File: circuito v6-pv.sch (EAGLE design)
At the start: 62 parts, among them IC1 LM324N

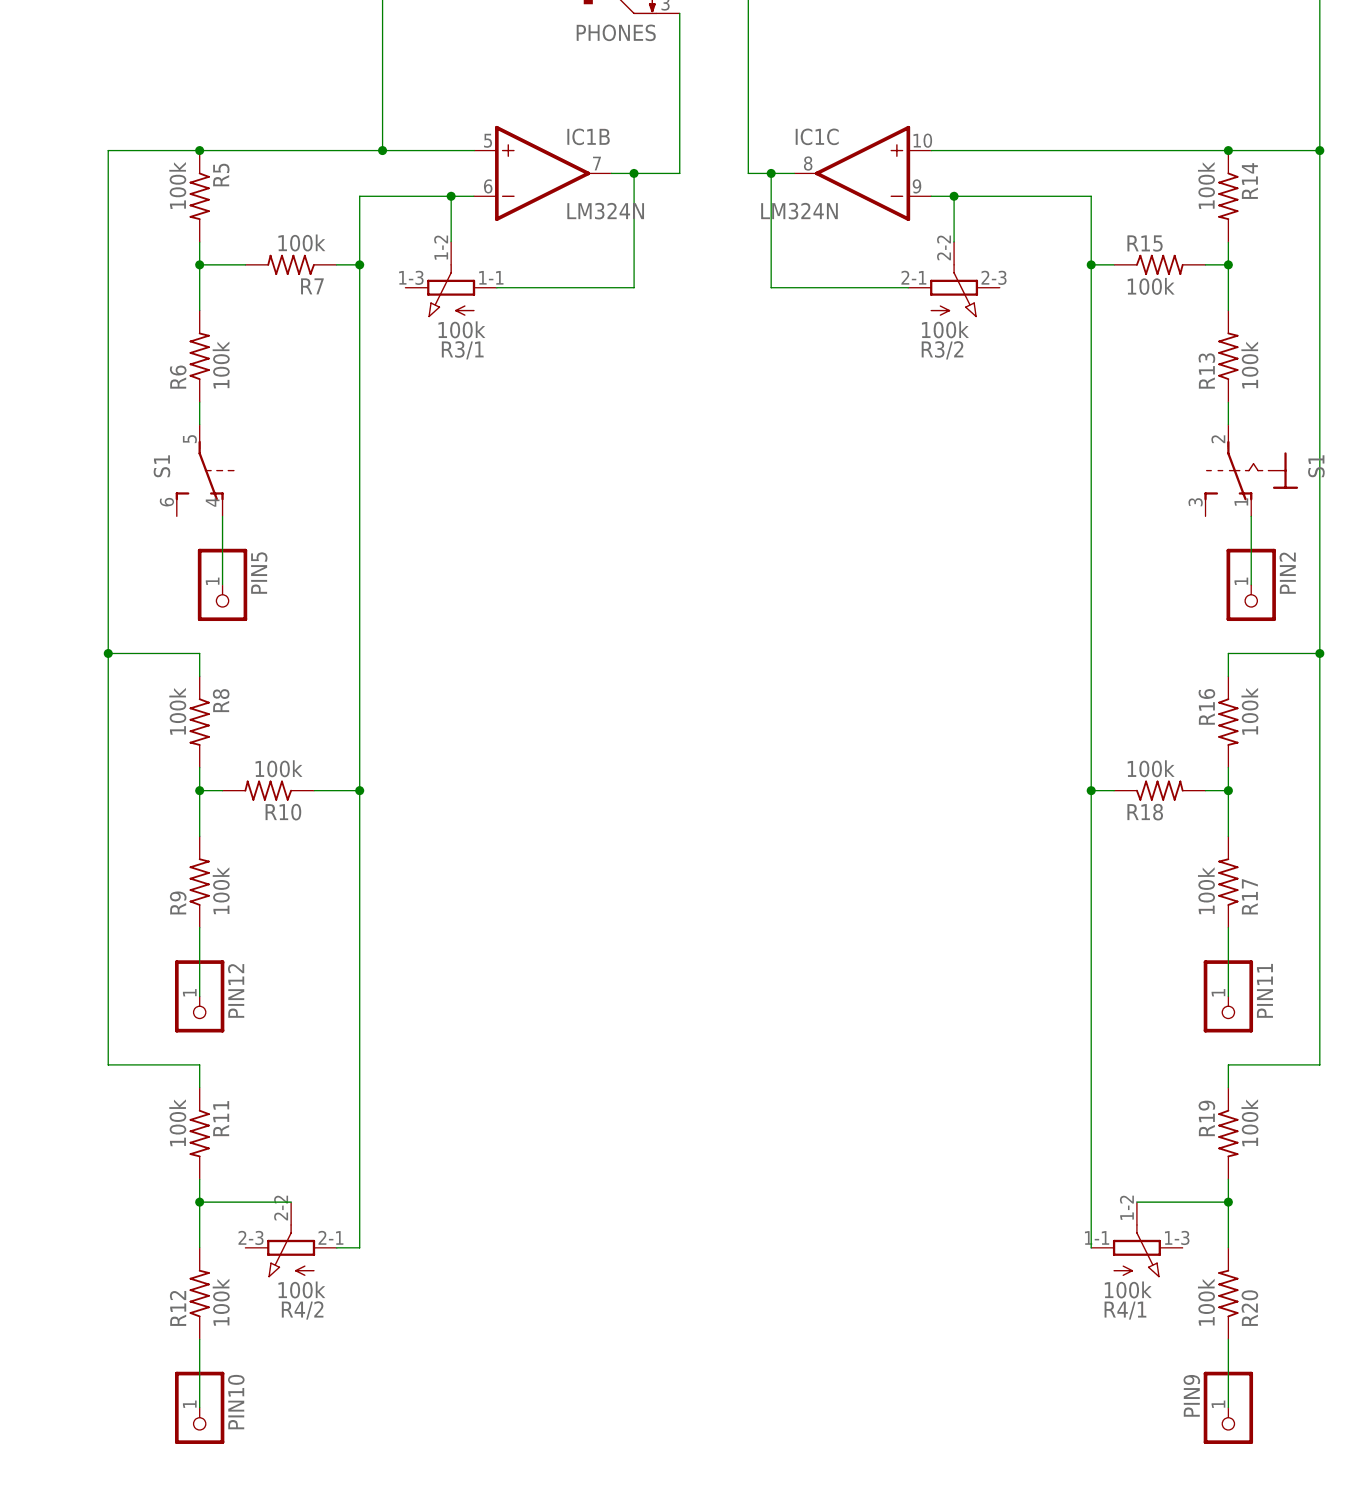
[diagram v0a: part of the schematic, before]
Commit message: Cambio de resistencias de 100k a 10k
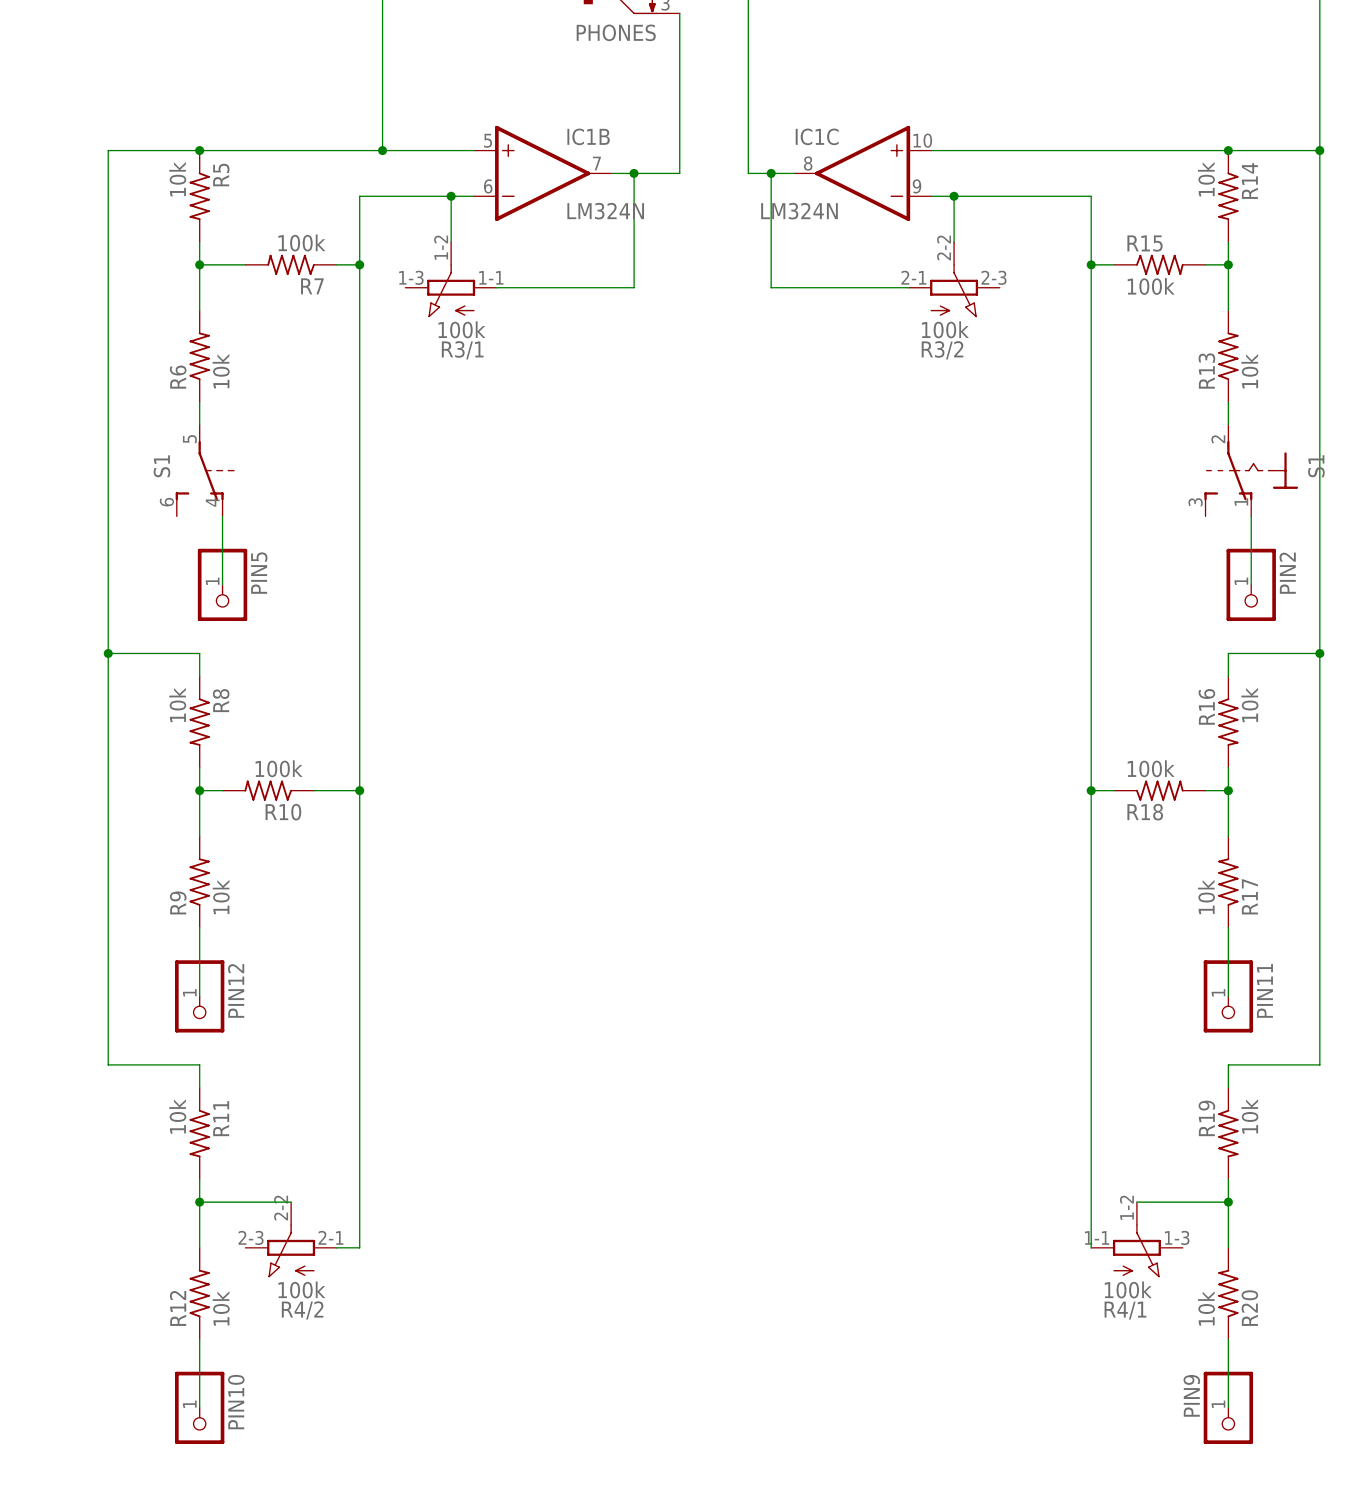
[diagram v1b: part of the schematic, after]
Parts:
- R11, R12, R13, R14, R16, R17, R19, R20, R5, R6, R8, R9: value 100k -> 10k
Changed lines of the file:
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@@
 <attribute name="SPICEPREFIX" value="J"/>
 </part>
-<part name="R5" library="rcl" library_urn="urn:adsk.eagle:library:334" deviceset="R-US_" device="0207/7" package3d_urn="urn:adsk.eagle:package:23493/1" value="100k">
+<part name="R5" library="rcl" library_urn="urn:adsk.eagle:library:334" deviceset="R-US_" device="0207/7" package3d_urn="urn:adsk.eagle:package:23493/1" value="10k">
 <spice>
 <pinmapping isusermap="yes" isdevicewide="yes">
@@
 </spice>
 </part>
-<part name="R6" library="rcl" library_urn="urn:adsk.eagle:library:334" deviceset="R-US_" device="0207/7" package3d_urn="urn:adsk.eagle:package:23493/1" value="100k">
+<part name="R6" library="rcl" library_urn="urn:adsk.eagle:library:334" deviceset="R-US_" device="0207/7" package3d_urn="urn:adsk.eagle:package:23493/1" value="10k">
 <spice>
 <pinmapping isusermap="yes" isdevicewide="yes">
@@
 <attribute name="SPICEPREFIX" value="X"/>
 </part>
-<part name="R8" library="rcl" library_urn="urn:adsk.eagle:library:334" deviceset="R-US_" device="0207/7" package3d_urn="urn:adsk.eagle:package:23493/1" value="100k">
+<part name="R8" library="rcl" library_urn="urn:adsk.eagle:library:334" deviceset="R-US_" device="0207/7" package3d_urn="urn:adsk.eagle:package:23493/1" value="10k">
 <spice>
 <pinmapping isusermap="yes" isdevicewide="yes">
@@
 </spice>
 </part>
-<part name="R9" library="rcl" library_urn="urn:adsk.eagle:library:334" deviceset="R-US_" device="0207/7" package3d_urn="urn:adsk.eagle:package:23493/1" value="100k">
+<part name="R9" library="rcl" library_urn="urn:adsk.eagle:library:334" deviceset="R-US_" device="0207/7" package3d_urn="urn:adsk.eagle:package:23493/1" value="10k">
 <spice>
 <pinmapping isusermap="yes" isdevicewide="yes">
@@
 <attribute name="SPICEPREFIX" value="X"/>
 </part>
-<part name="R11" library="rcl" library_urn="urn:adsk.eagle:library:334" deviceset="R-US_" device="0207/7" package3d_urn="urn:adsk.eagle:package:23493/1" value="100k">
+<part name="R11" library="rcl" library_urn="urn:adsk.eagle:library:334" deviceset="R-US_" device="0207/7" package3d_urn="urn:adsk.eagle:package:23493/1" value="10k">
 <spice>
 <pinmapping isusermap="yes" isdevicewide="yes">
@@
 </spice>
 </part>
-<part name="R12" library="rcl" library_urn="urn:adsk.eagle:library:334" deviceset="R-US_" device="0207/7" package3d_urn="urn:adsk.eagle:package:23493/1" value="100k">
+<part name="R12" library="rcl" library_urn="urn:adsk.eagle:library:334" deviceset="R-US_" device="0207/7" package3d_urn="urn:adsk.eagle:package:23493/1" value="10k">
 <spice>
 <pinmapping isusermap="yes" isdevicewide="yes">
@@
 <attribute name="SPICEPREFIX" value="X"/>
 </part>
-<part name="R13" library="rcl" library_urn="urn:adsk.eagle:library:334" deviceset="R-US_" device="0207/7" package3d_urn="urn:adsk.eagle:package:23493/1" value="100k">
+<part name="R13" library="rcl" library_urn="urn:adsk.eagle:library:334" deviceset="R-US_" device="0207/7" package3d_urn="urn:adsk.eagle:package:23493/1" value="10k">
 <spice>
 <pinmapping isusermap="yes" isdevicewide="yes">
@@
 </spice>
 </part>
-<part name="R14" library="rcl" library_urn="urn:adsk.eagle:library:334" deviceset="R-US_" device="0207/7" package3d_urn="urn:adsk.eagle:package:23493/1" value="100k">
+<part name="R14" library="rcl" library_urn="urn:adsk.eagle:library:334" deviceset="R-US_" device="0207/7" package3d_urn="urn:adsk.eagle:package:23493/1" value="10k">
 <spice>
 <pinmapping isusermap="yes" isdevicewide="yes">
@@
 <attribute name="SPICEPREFIX" value="X"/>
 </part>
-<part name="R16" library="rcl" library_urn="urn:adsk.eagle:library:334" deviceset="R-US_" device="0207/7" package3d_urn="urn:adsk.eagle:package:23493/1" value="100k">
+<part name="R16" library="rcl" library_urn="urn:adsk.eagle:library:334" deviceset="R-US_" device="0207/7" package3d_urn="urn:adsk.eagle:package:23493/1" value="10k">
 <spice>
 <pinmapping isusermap="yes" isdevicewide="yes">
@@
 </spice>
 </part>
-<part name="R17" library="rcl" library_urn="urn:adsk.eagle:library:334" deviceset="R-US_" device="0207/7" package3d_urn="urn:adsk.eagle:package:23493/1" value="100k">
+<part name="R17" library="rcl" library_urn="urn:adsk.eagle:library:334" deviceset="R-US_" device="0207/7" package3d_urn="urn:adsk.eagle:package:23493/1" value="10k">
 <spice>
 <pinmapping isusermap="yes" isdevicewide="yes">
@@
 <attribute name="SPICEPREFIX" value="X"/>
 </part>
-<part name="R19" library="rcl" library_urn="urn:adsk.eagle:library:334" deviceset="R-US_" device="0207/7" package3d_urn="urn:adsk.eagle:package:23493/1" value="100k">
+<part name="R19" library="rcl" library_urn="urn:adsk.eagle:library:334" deviceset="R-US_" device="0207/7" package3d_urn="urn:adsk.eagle:package:23493/1" value="10k">
 <spice>
 <pinmapping isusermap="yes" isdevicewide="yes">
@@
 </spice>
 </part>
-<part name="R20" library="rcl" library_urn="urn:adsk.eagle:library:334" deviceset="R-US_" device="0207/7" package3d_urn="urn:adsk.eagle:package:23493/1" value="100k">
+<part name="R20" library="rcl" library_urn="urn:adsk.eagle:library:334" deviceset="R-US_" device="0207/7" package3d_urn="urn:adsk.eagle:package:23493/1" value="10k">
 <spice>
 <pinmapping isusermap="yes" isdevicewide="yes">

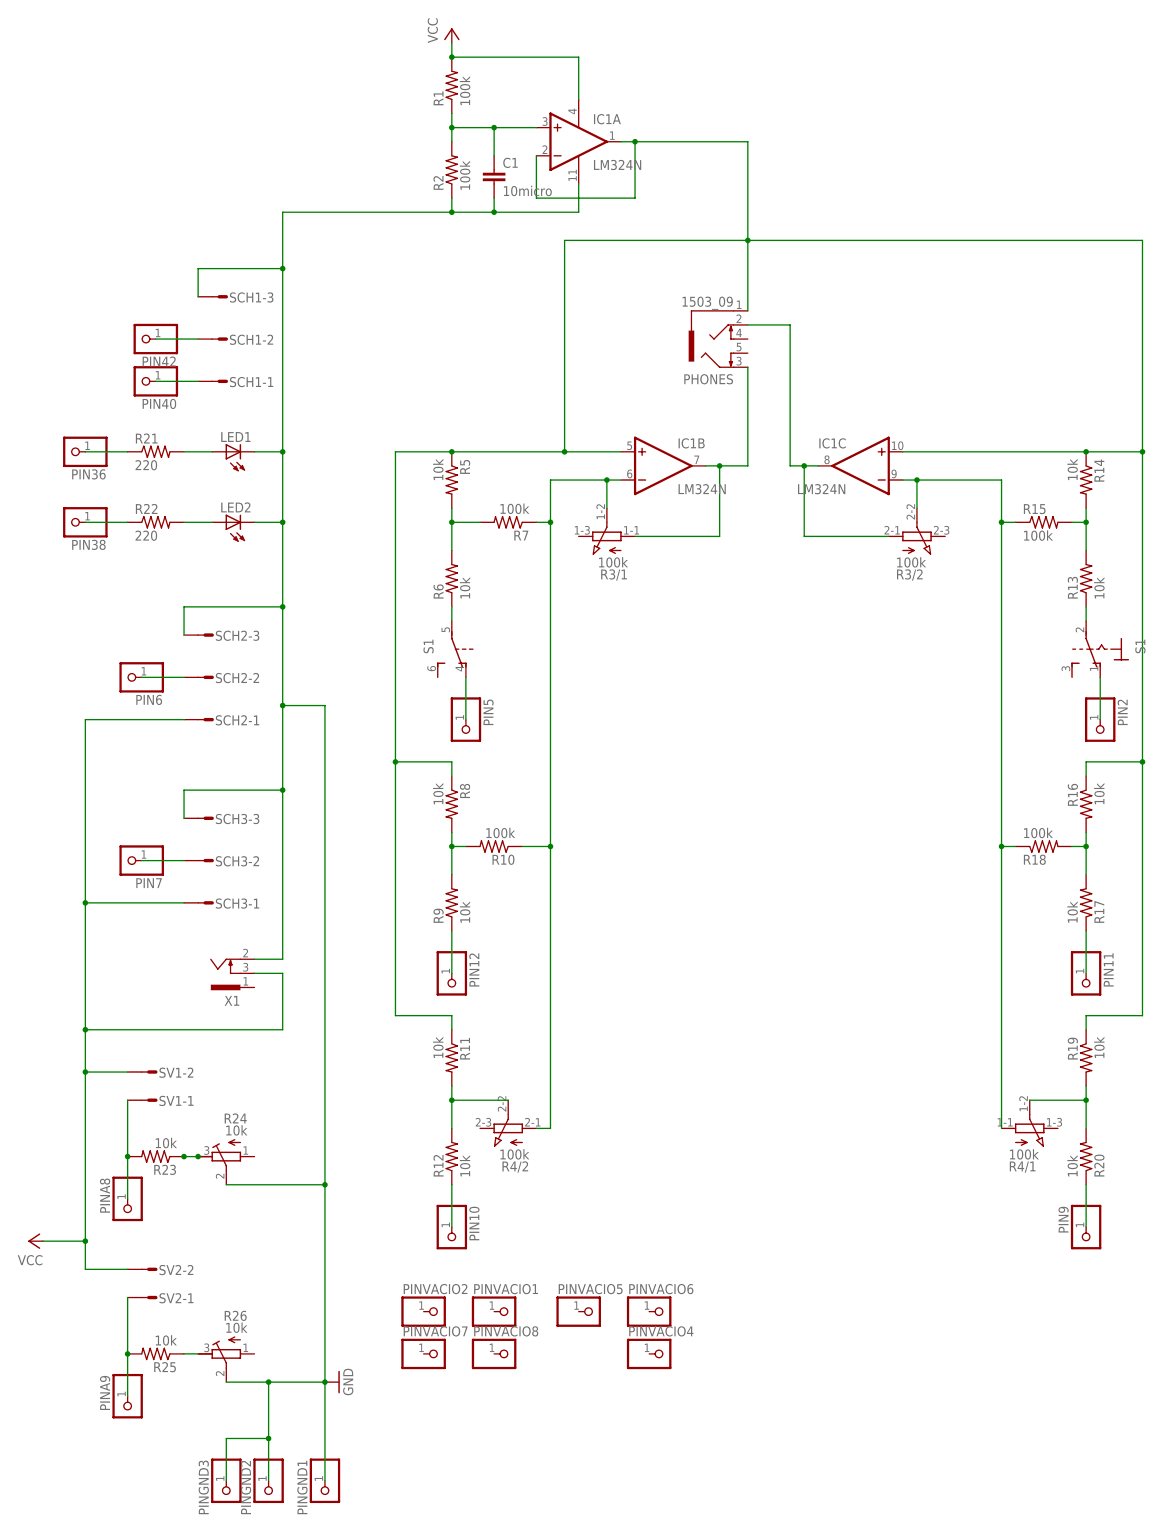
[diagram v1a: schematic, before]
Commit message: ACTUALIZACION CIRCUITO
Cambios

1- Chequeo de pines/canales/izq y der: 

IZQ - B - 12,9 Y 2
DER - A - 11,10Y5

2- CONEXION TIERRA VIRTUAL A PIN A11

3- CAMBIO DE RESISTENCIAS PARA EL PIN DEL RUIDO

EL POTE PASA A SER DOS Rs DE 100K FIJAS
R11 Y R19 TENIAN 10K Y AHORA TIENEN 1K
R12 Y R20 TENIAN 10K Y AHORA TIENEN 20K

4- SE AGREGAN RESISTENCIAS EN LAS PATAS + DE LOS OPAMPS DE AUDIO (IZQ Y DER)

UNA A TIERRA VIRTUAL DE 10K
OTRA A TIERRA NORMAL DE 100K
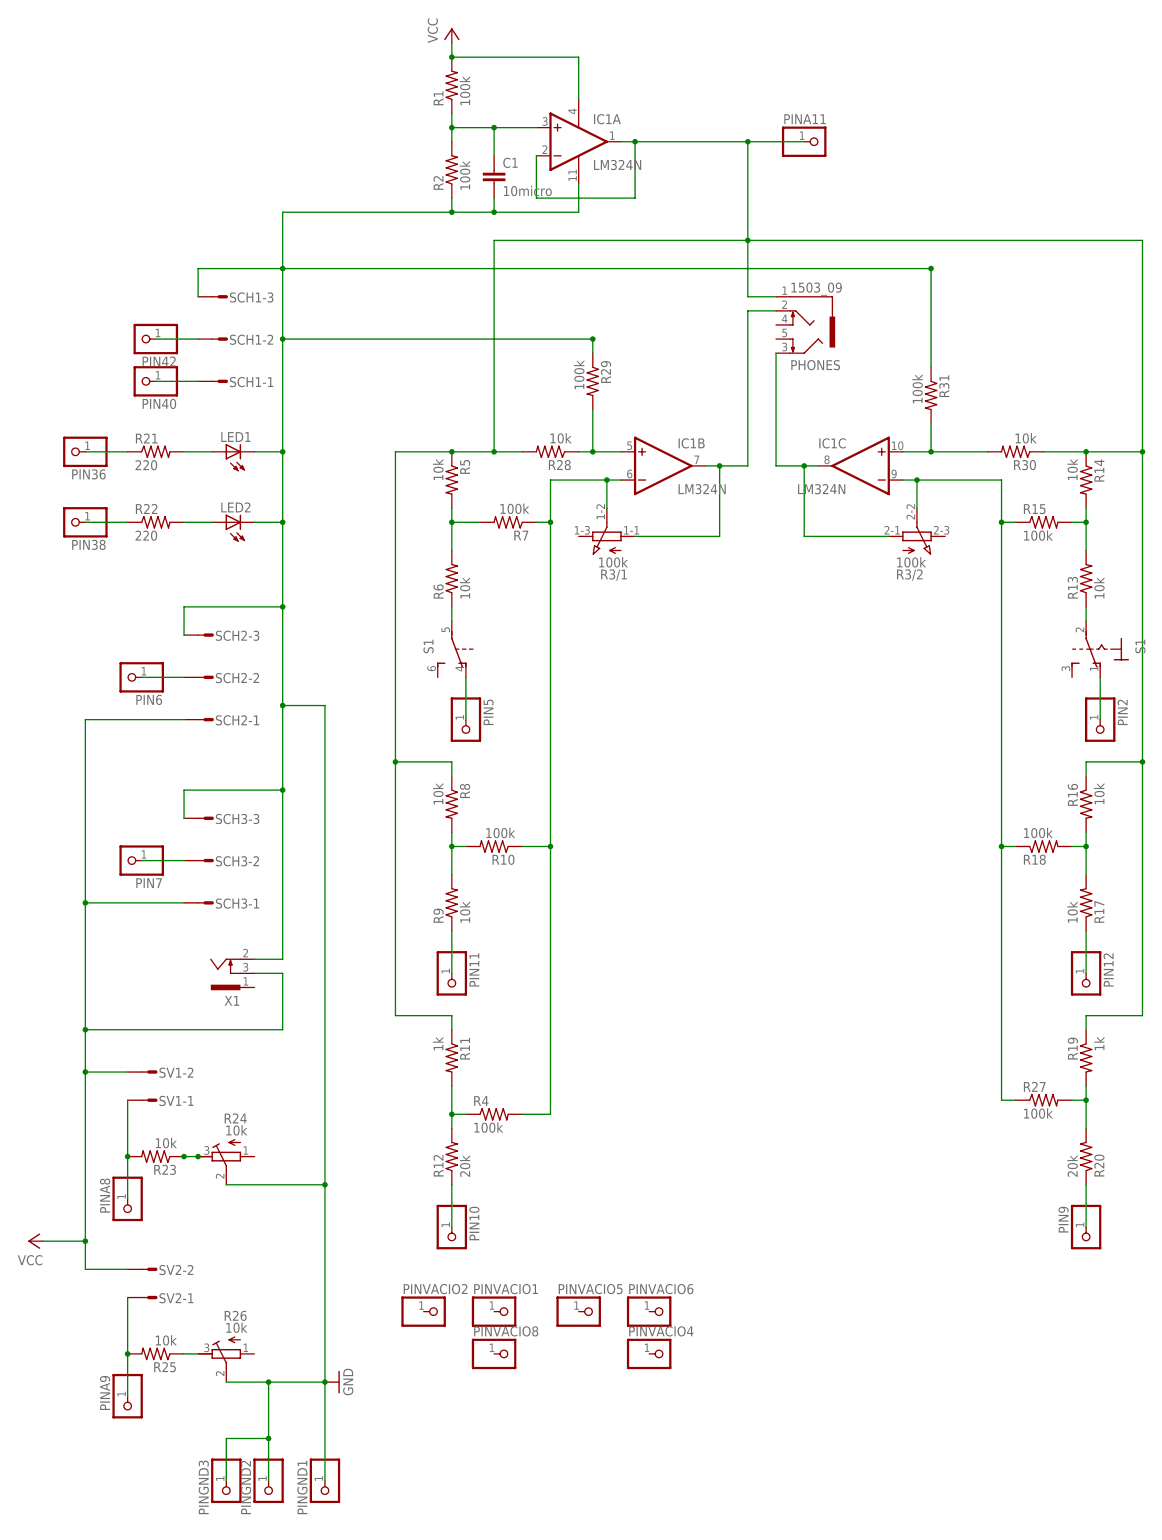
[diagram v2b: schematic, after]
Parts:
- removed PINVACIO7: (no value), pinhead:PINHD-1X1
- added PINA11: (no value), pinhead:PINHD-1X1
- added R27, R29, R31: 100k, rcl:R-US_0207/7
- added R28, R30: 10k, rcl:R-US_0207/7
- R11, R19: value 10k -> 1k
- R12, R20: value 10k -> 20k
- R4: device pot:3RP/1610G -> rcl:R-US_0207/7; SPICEPREFIX J -> (none)
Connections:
- new net N$10: IC1C.+IN, R30.2, R31.2
- new net N$17: IC1B.+IN, R28.1, R29.2
- net GND: now also R29.1, R31.1
- net N$11: now also R4.1; no longer R4/2.S
- net N$13: now also R27.1; no longer R4/1.A
- net N$18: now also R27.2; no longer R4/1.S
- net N$20: now also PIN12.1; no longer PIN11.1
- net N$3: now also PIN11.1; no longer PIN12.1
- net N$30: now also PHONES.3; no longer PHONES.2
- net N$37: now also PHONES.2; no longer PHONES.3
- net N$4: now also R4.2; no longer R4/2.A
- net N$8: now also PINA11.1, R28.2, R30.1; no longer IC1B.+IN, IC1C.+IN
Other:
- moved on the sheet: PHONES, PIN11, PIN12
